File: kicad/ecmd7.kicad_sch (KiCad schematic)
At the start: 26 parts, among them J1 PMOD_SPI_ENC, J2 PMOD_ADC_MPIO, J3 PMOD_DRV, J4 Conn_01x02_Socket, J5 Encoder, J7 RS422/BISS-C

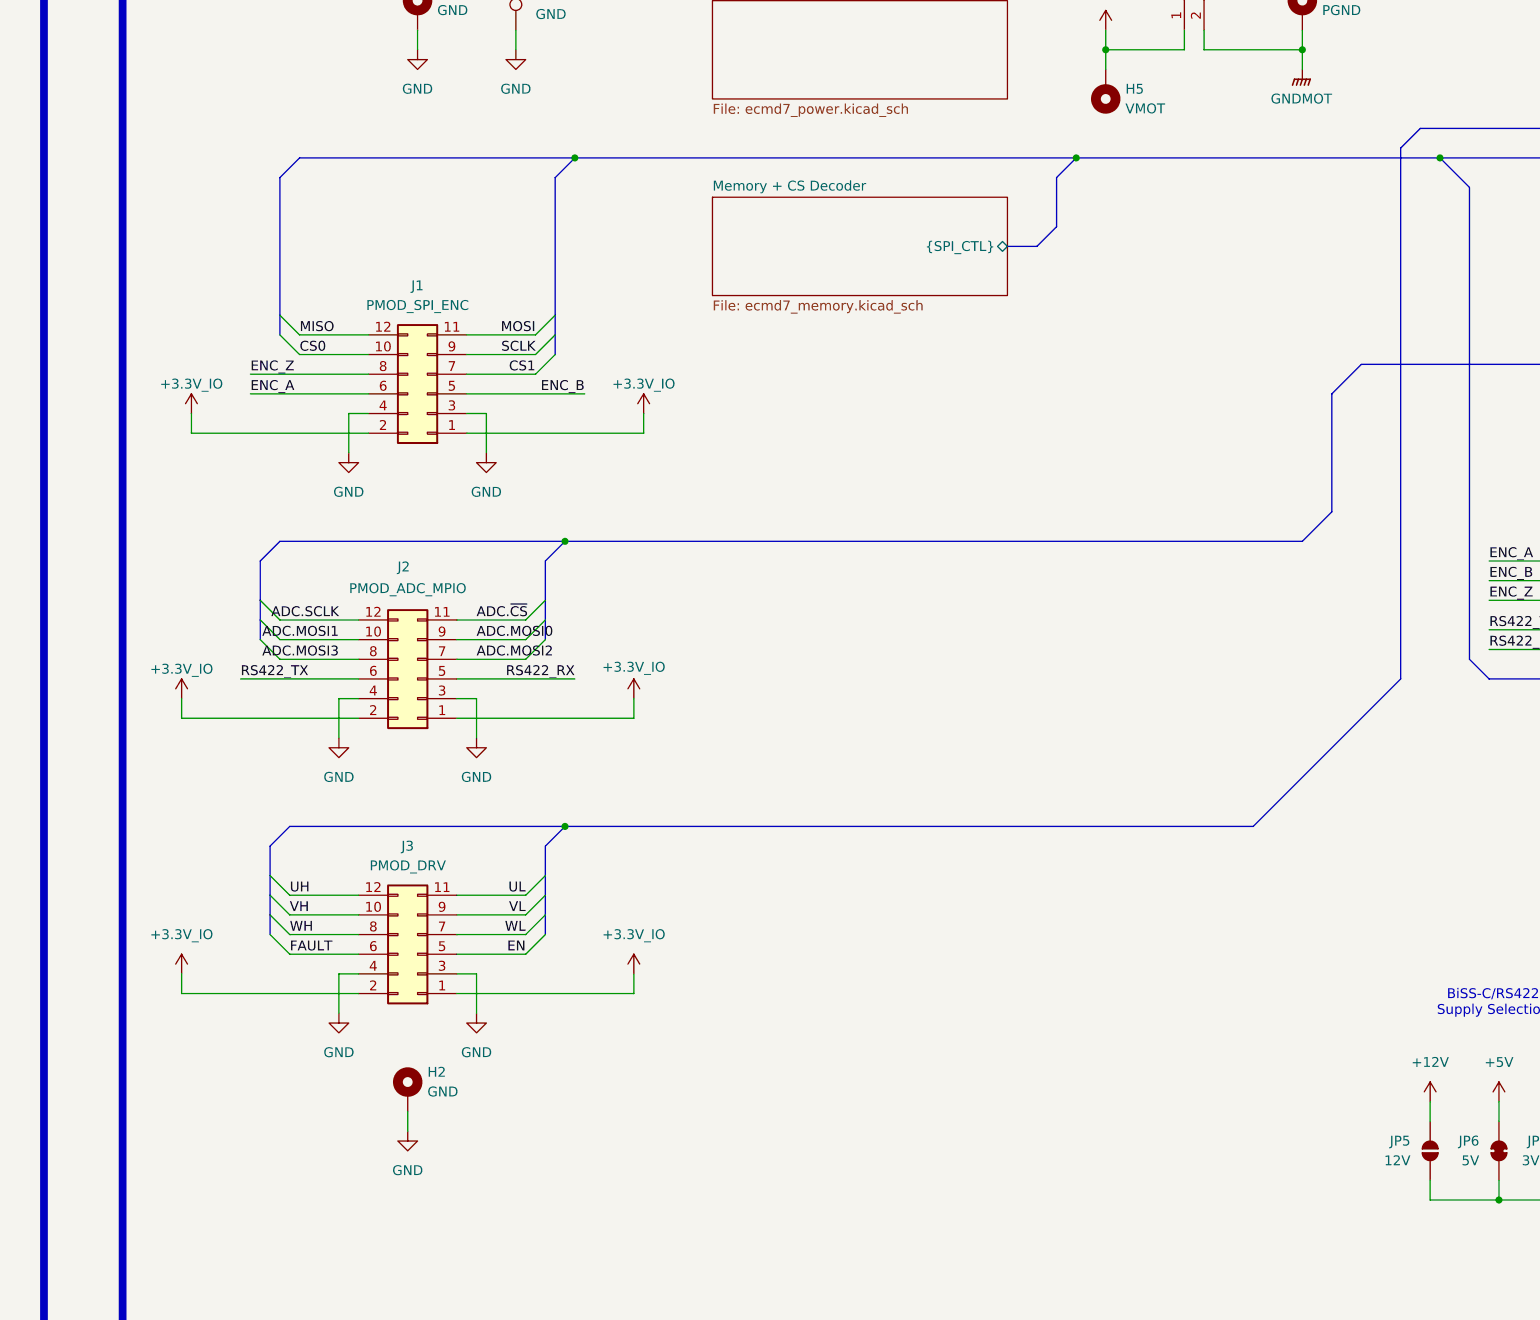
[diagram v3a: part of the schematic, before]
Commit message: General schematic cleanup
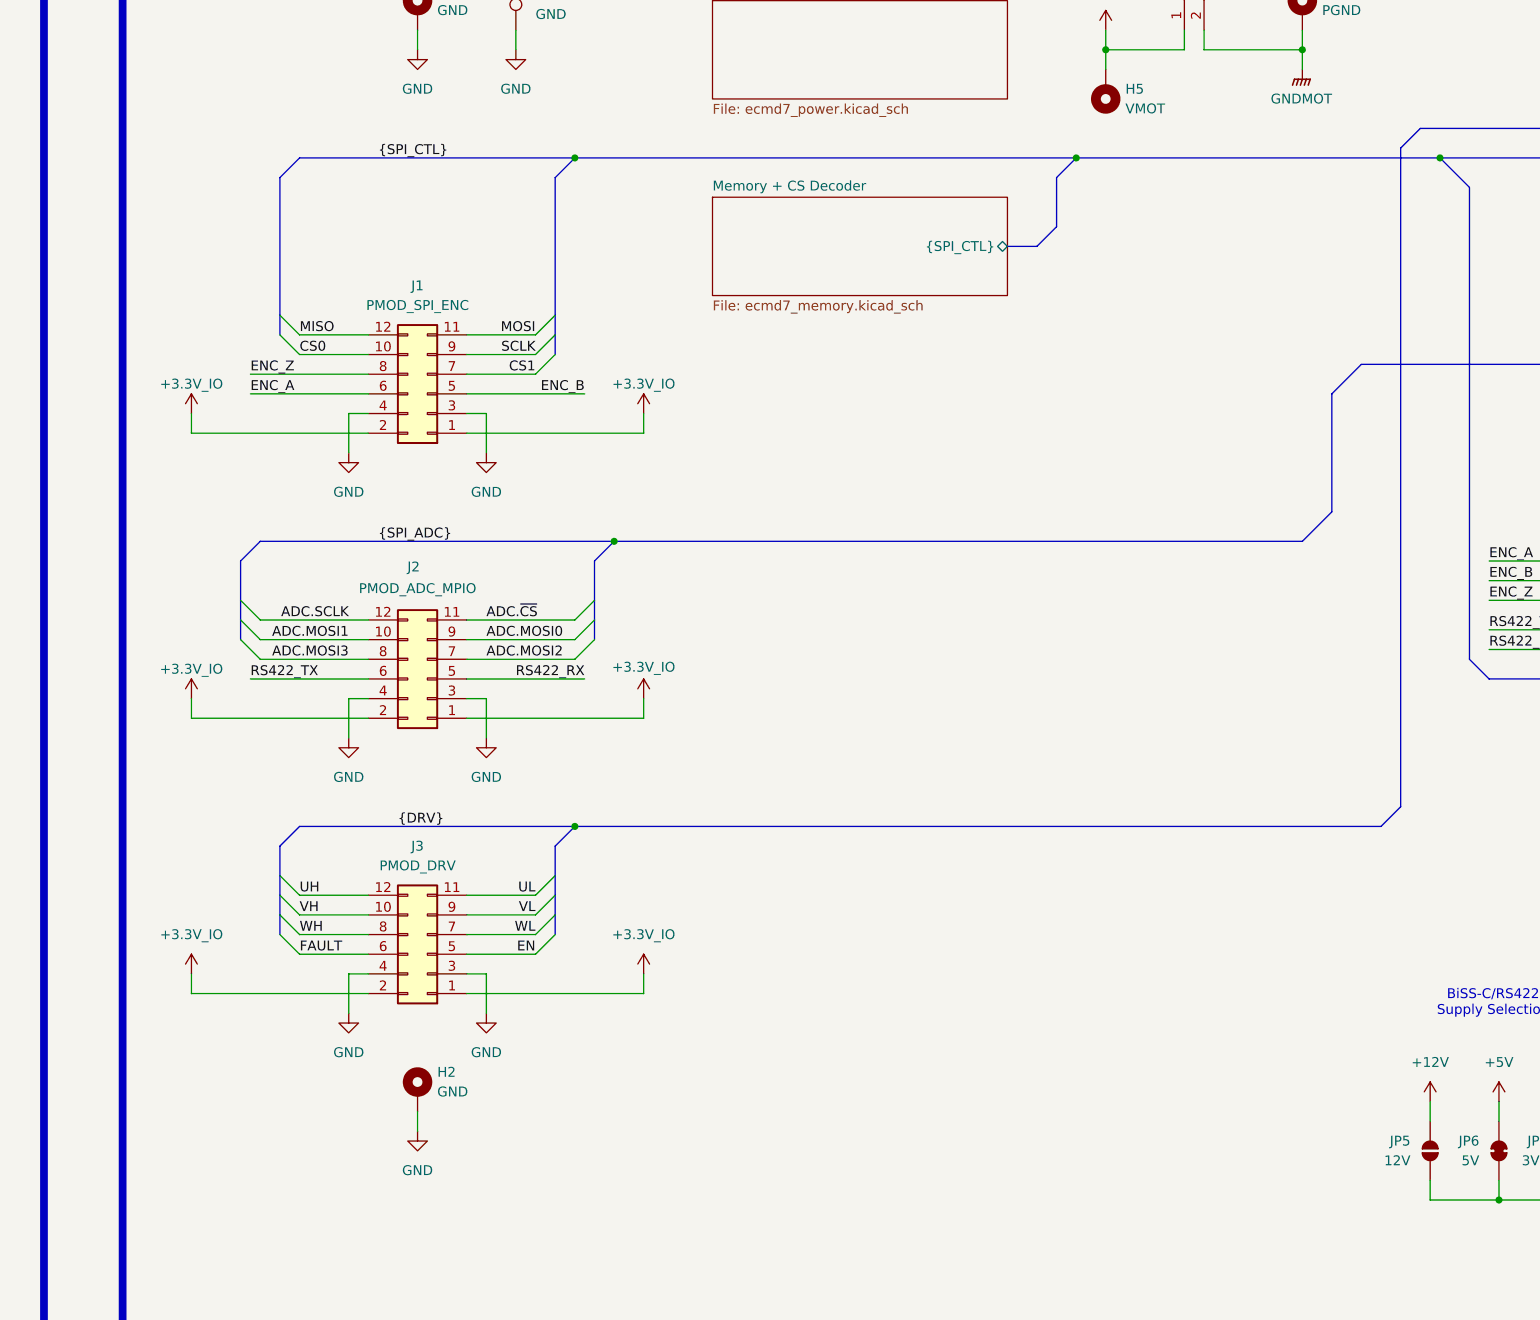
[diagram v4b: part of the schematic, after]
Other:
- moved on the sheet: H2, J2, J3

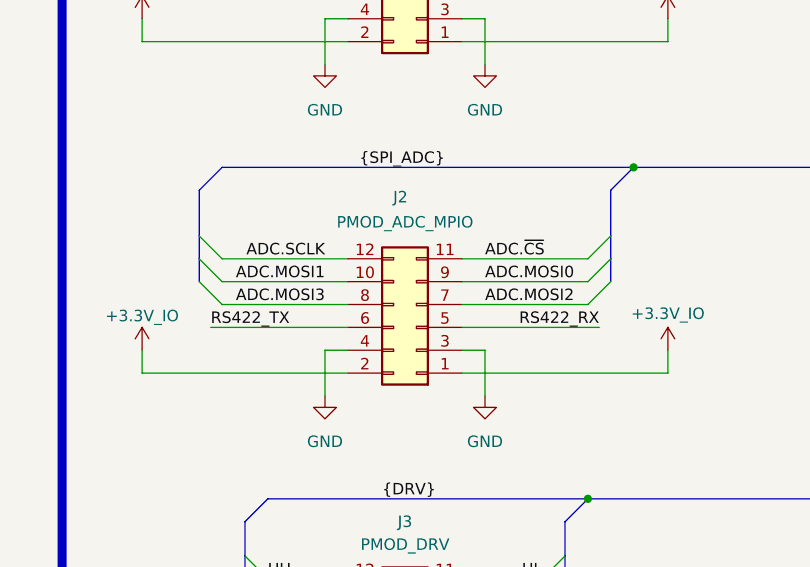
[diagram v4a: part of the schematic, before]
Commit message: Fix MOSI/MISO naming ADC
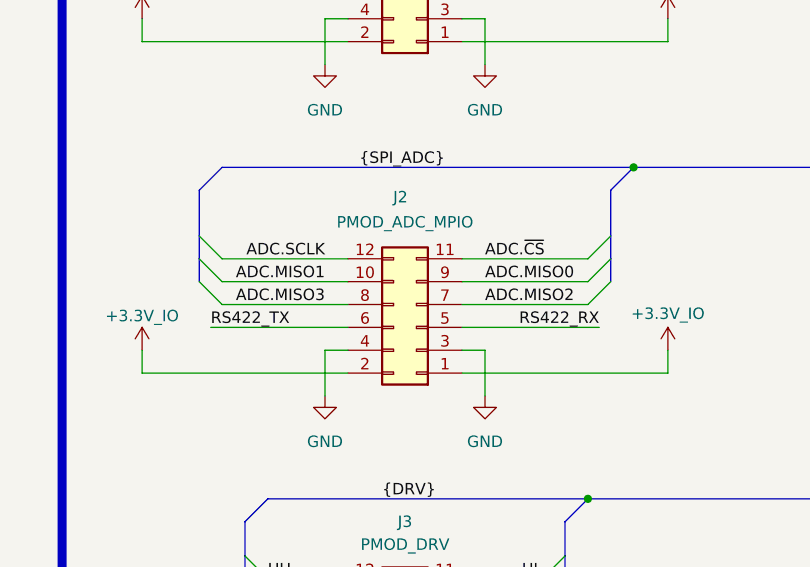
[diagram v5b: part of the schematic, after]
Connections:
- net ADC.MOSI0 renamed ADC.MISO0
- net ADC.MOSI1 renamed ADC.MISO1
- net ADC.MOSI2 renamed ADC.MISO2
- net ADC.MOSI3 renamed ADC.MISO3
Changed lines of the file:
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@@
 	)
 	(bus_alias "SPI_ADC"
-		(members "ADC.SCLK" "ADC.MISO" "ADC.MOSI[0..3]" "ADC.~{CS}")
+		(members "ADC.SCLK" "ADC.MOSI" "ADC.MISO[0..3]" "ADC.~{CS}")
 	)
 	(bus_alias "SPI_CTL"
@@
 		)
 	)
-	(label "ADC.MOSI0"
+	(label "ADC.MISO0"
 		(at 110.49 133.35 0)
 		(effects
@@
 		)
 	)
-	(label "ADC.MOSI1"
+	(label "ADC.MISO1"
 		(at 92.71 133.35 180)
 		(effects
@@
 		)
 	)
-	(label "ADC.MOSI2"
+	(label "ADC.MISO2"
 		(at 110.49 135.89 0)
 		(effects
@@
 		)
 	)
-	(label "ADC.MOSI3"
+	(label "ADC.MISO3"
 		(at 92.71 135.89 180)
 		(effects

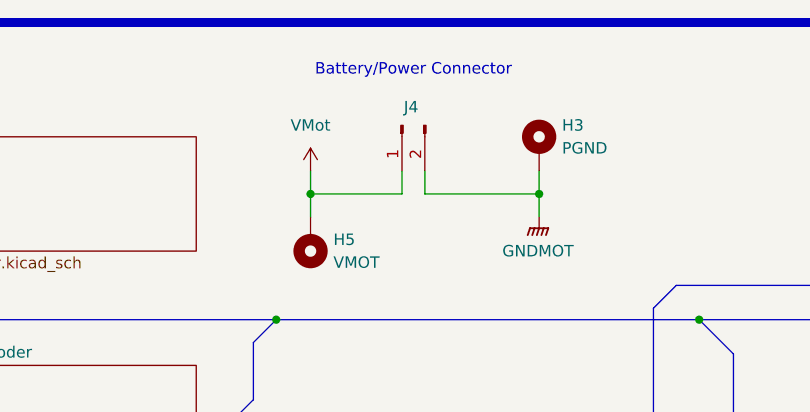
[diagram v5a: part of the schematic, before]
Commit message: Fix power connector polarity
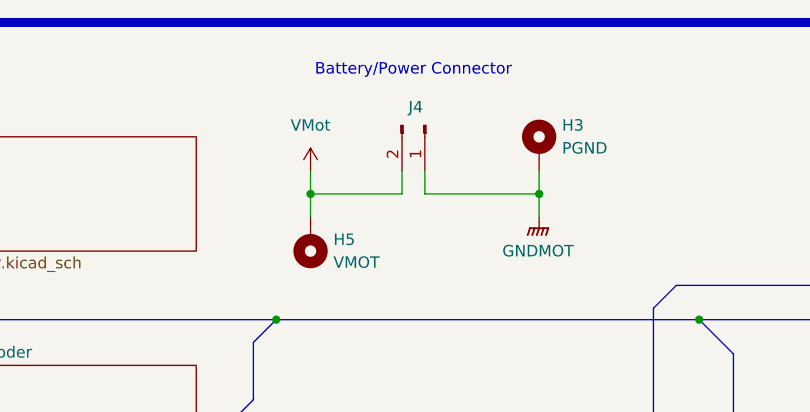
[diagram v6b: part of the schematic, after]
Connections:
- net GNDMOT: now also J4.1 (Pin_1); no longer J4.2 (Pin_2)
- net VMot: now also J4.2 (Pin_2); no longer J4.1 (Pin_1)
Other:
- moved on the sheet: J4
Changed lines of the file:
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@@
 	(symbol
 		(lib_id "Connector:Conn_01x02_Pin")
-		(at 200.66 49.53 90)
-		(mirror x)
+		(at 203.2 49.53 270)
 		(unit 1)
 		(exclude_from_sim no)
@@
 		(dnp no)
 		(property "Reference" "J4"
-			(at 201.676 47.498 90)
+			(at 202.184 47.498 90)
 			(effects
 				(font
@@
 		)
 		(property "Value" "Conn_01x02_Socket"
-			(at 198.12 50.165 0)
+			(at 205.74 50.165 0)
 			(effects
 				(font
@@
 		)
 		(property "Footprint" "Connector_AMASS:AMASS_XT60-M_1x02_P7.20mm_Vertical"
-			(at 200.66 49.53 0)
+			(at 203.2 49.53 0)
 			(effects
 				(font
@@
 		)
 		(property "Datasheet" "~"
-			(at 200.66 49.53 0)
+			(at 203.2 49.53 0)
 			(effects
 				(font
@@
 		)
 		(property "Description" "Generic connector, single row, 01x02, script generated"
-			(at 200.66 49.53 0)
+			(at 203.2 49.53 0)
 			(effects
 				(font
@@
 		)
 		(property "Sim.Type" ""
-			(at 200.66 49.53 0)
+			(at 203.2 49.53 0)
 			(effects
 				(font
